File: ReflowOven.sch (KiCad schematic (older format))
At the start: 0 parts

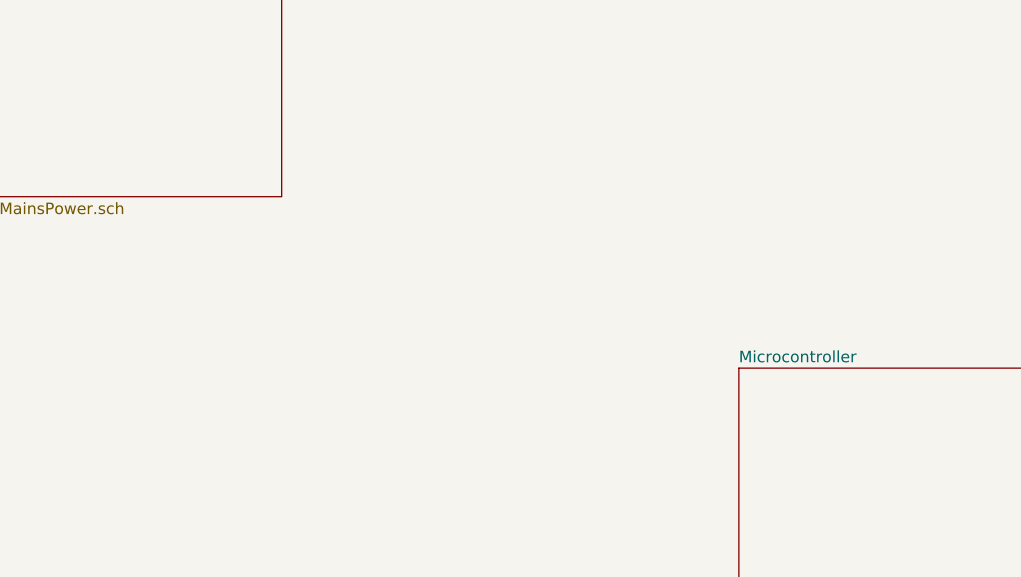
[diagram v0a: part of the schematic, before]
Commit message: Added RELAY_SET to top-level
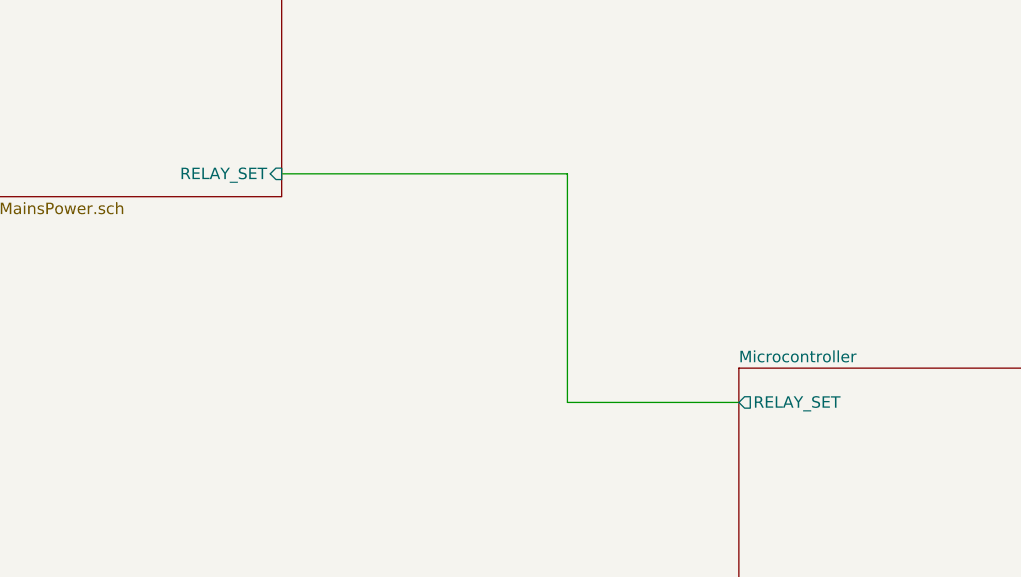
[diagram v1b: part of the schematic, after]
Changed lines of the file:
@@
 $Descr A4 11693 8268
 encoding utf-8
-Sheet 1 5
+Sheet 1 6
 Title ""
 Date ""
@@
 F0 "MainsPower" 50
 F1 "MainsPower.sch" 50
+F2 "RELAY_SET" I R 3250 2600 50
 $EndSheet
 $Sheet
@@
 F0 "Microcontroller" 50
 F1 "Microcontroller.sch" 50
+F2 "RELAY_SET" O L 5250 3600 50
 $EndSheet
 $Sheet
@@
 F1 "Communication.sch" 50
 $EndSheet
+Wire Wire Line
+	4500 3600 4500 2600
+Wire Wire Line
+	4500 2600 3250 2600
+Wire Wire Line
+	4500 3600 5250 3600
 $EndSCHEMATC

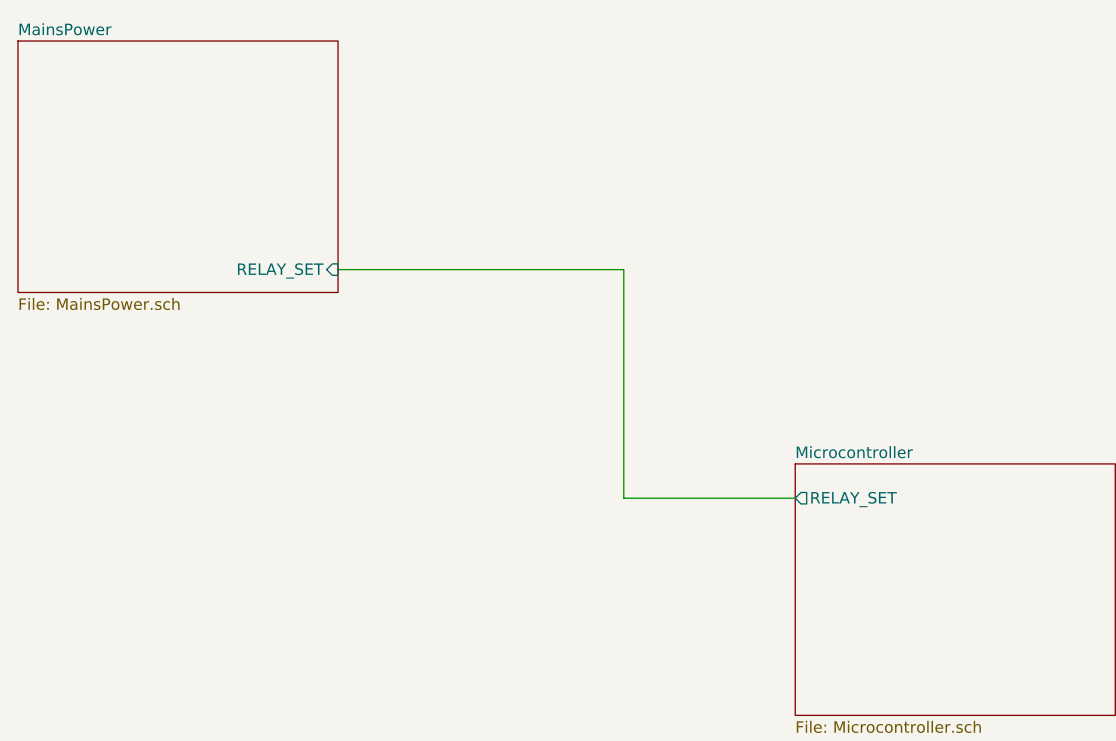
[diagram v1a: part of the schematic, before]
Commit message: Added current sense
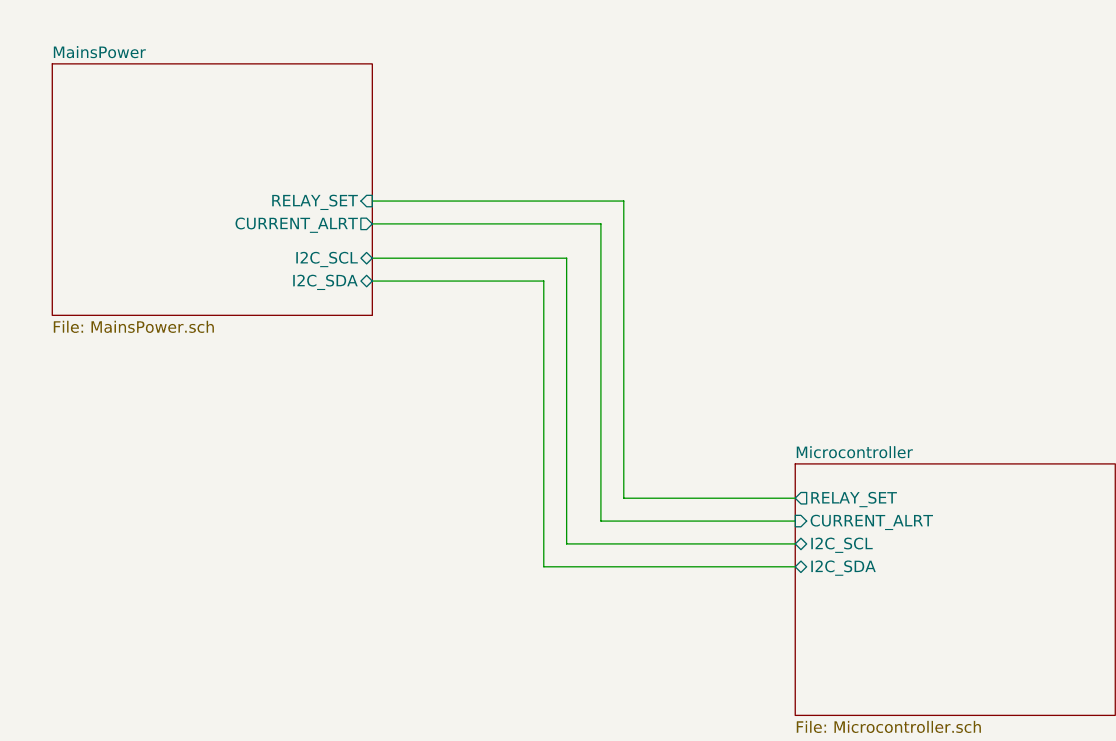
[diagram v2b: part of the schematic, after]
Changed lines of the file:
@@
 	10200 6950 11200 6950
-$Sheet
-S 1850 1600 1400 1100
-U 5F641519
-F0 "MainsPower" 50
-F1 "MainsPower.sch" 50
-F2 "RELAY_SET" I R 3250 2600 50
-$EndSheet
 $Sheet
 S 5250 3450 1400 1100
@@
 F1 "Microcontroller.sch" 50
 F2 "RELAY_SET" O L 5250 3600 50
+F3 "CURRENT_ALRT" I L 5250 3700 50
+F4 "I2C_SCL" B L 5250 3800 50
+F5 "I2C_SDA" B L 5250 3900 50
 $EndSheet
 $Sheet
@@
 $EndSheet
 Wire Wire Line
-	4500 3600 4500 2600
+	4500 3600 4500 2300
 Wire Wire Line
-	4500 2600 3250 2600
+	4500 2300 3400 2300
 Wire Wire Line
 	4500 3600 5250 3600
+$Sheet
+S 2000 1700 1400 1100
+U 5F641519
+F0 "MainsPower" 50
+F1 "MainsPower.sch" 50
+F2 "RELAY_SET" I R 3400 2300 50
+F3 "CURRENT_ALRT" O R 3400 2400 50
+F4 "I2C_SCL" B R 3400 2550 50
+F5 "I2C_SDA" B R 3400 2650 50
+$EndSheet
+Wire Wire Line
+	5250 3700 4400 3700
+Wire Wire Line
+	4400 3700 4400 2400
+Wire Wire Line
+	4400 2400 3400 2400
+Wire Wire Line
+	3400 2550 4250 2550
+Wire Wire Line
+	4250 2550 4250 3800
+Wire Wire Line
+	4250 3800 5250 3800
+Wire Wire Line
+	4150 3900 4150 2650
+Wire Wire Line
+	4150 2650 3400 2650
+Wire Wire Line
+	4150 3900 5250 3900
 $EndSCHEMATC

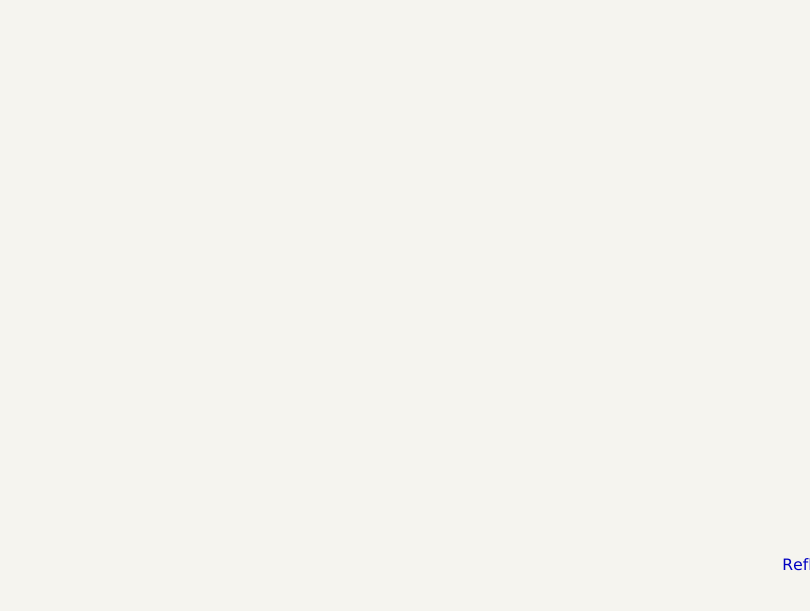
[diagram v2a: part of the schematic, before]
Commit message: Added communication interfaces
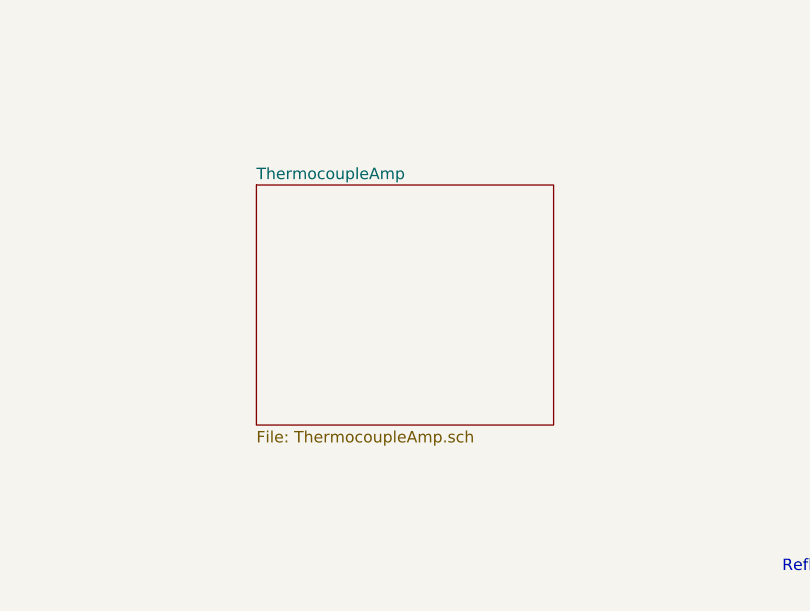
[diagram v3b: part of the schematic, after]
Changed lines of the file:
@@
 Wire Wire Line
 	4150 3900 5250 3900
+$Sheet
+S 5100 5800 1300 1050
+U 5F67E1E1
+F0 "ThermocoupleAmp" 50
+F1 "ThermocoupleAmp.sch" 50
+$EndSheet
 $EndSCHEMATC

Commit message: Added top level changes
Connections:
- wire segments 12 -> 14
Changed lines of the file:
@@
 $Descr A4 11693 8268
 encoding utf-8
-Sheet 1 6
+Sheet 1 7
 Title ""
 Date ""
@@
 	10200 6950 11200 6950
 $Sheet
-S 5250 3450 1400 1100
+S 5250 3450 1700 1500
 U 5F6415F0
 F0 "Microcontroller" 50
@@
 F4 "I2C_SCL" B L 5250 3800 50
 F5 "I2C_SDA" B L 5250 3900 50
+F6 "USB_DP" B R 6950 4850 50
+F7 "USB_DM" B R 6950 4750 50
+F8 "UART_TX" O R 6950 4550 50
+F9 "UART_RX" I R 6950 4450 50
+F10 "UART_RTS" B R 6950 4350 50
+F11 "UART_CTS" B R 6950 4250 50
+F12 "SPI_SCK" B R 6950 3850 50
+F13 "SPI_MISO" B R 6950 3750 50
+F14 "SPI_MOSI" B R 6950 3650 50
+F15 "SPI_NSS" B R 6950 3550 50
+F16 "CANL" B R 6950 4100 50
+F17 "CANH" B R 6950 4000 50
 $EndSheet
 $Sheet
@@
 	4150 3900 5250 3900
 $Sheet
-S 5100 5800 1300 1050
+S 1950 3600 1300 1050
 U 5F67E1E1
 F0 "ThermocoupleAmp" 50
 F1 "ThermocoupleAmp.sch" 50
 $EndSheet
+Wire Wire Line
+	4250 3800 3350 3800
+Connection ~ 4250 3800
+Wire Wire Line
+	4150 3900 3350 3900
+Connection ~ 4150 3900
 $EndSCHEMATC

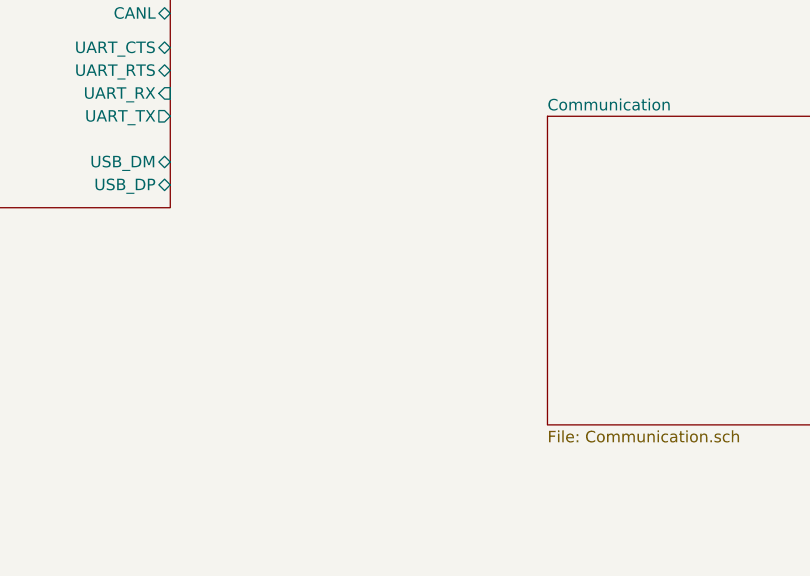
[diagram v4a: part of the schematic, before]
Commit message: Added USB Connector
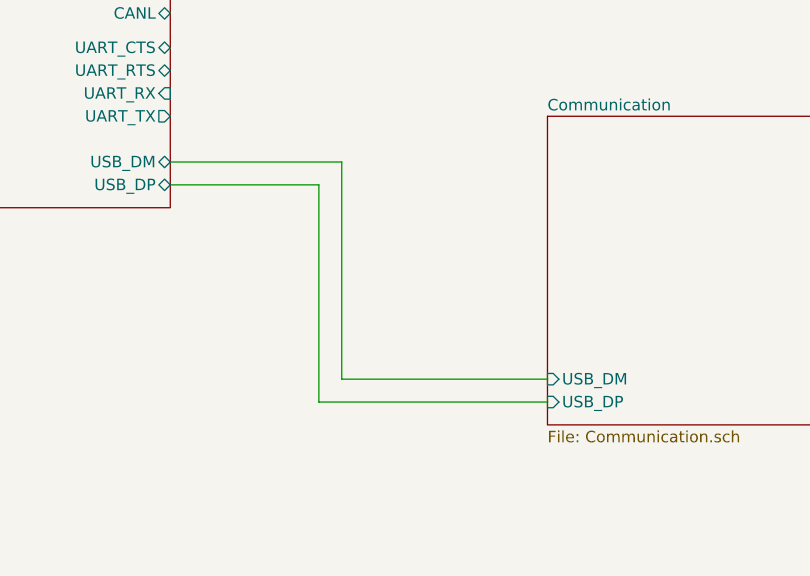
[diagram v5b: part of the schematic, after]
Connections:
- wire segments 14 -> 20
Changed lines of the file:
@@
 F0 "Communication" 50
 F1 "Communication.sch" 50
+F2 "USB_DP" I L 8600 5800 50
+F3 "USB_DM" I L 8600 5700 50
 $EndSheet
 Wire Wire Line
@@
 	4150 3900 3350 3900
 Connection ~ 4150 3900
+Wire Wire Line
+	6950 4850 7600 4850
+Wire Wire Line
+	7600 4850 7600 5800
+Wire Wire Line
+	7600 5800 8600 5800
+Wire Wire Line
+	8600 5700 7700 5700
+Wire Wire Line
+	7700 5700 7700 4750
+Wire Wire Line
+	7700 4750 6950 4750
 $EndSCHEMATC
